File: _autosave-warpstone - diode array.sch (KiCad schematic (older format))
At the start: 89 parts, among them SW1 SW_Push, U1 ProMicro

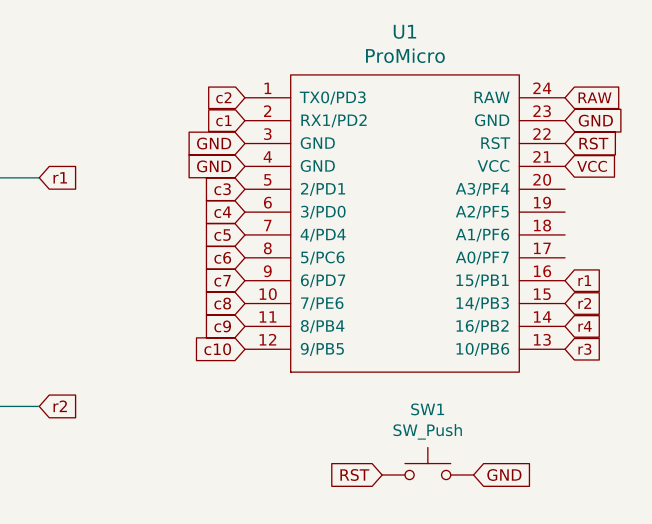
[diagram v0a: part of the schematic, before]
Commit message: overhaul
total overhaul to the design of the board
case design now available
protos en route
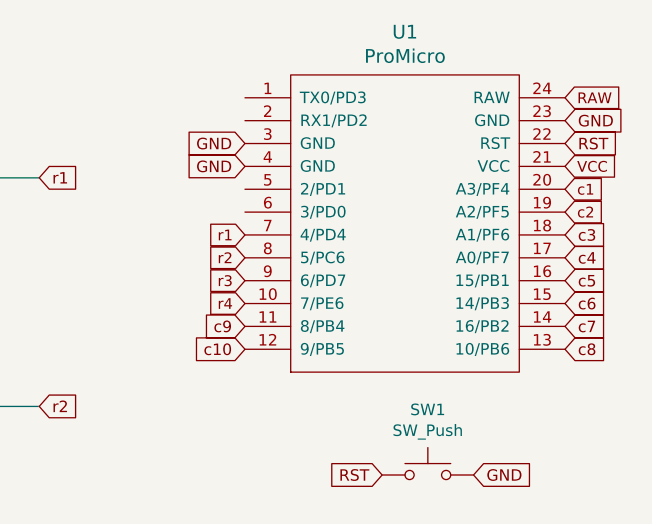
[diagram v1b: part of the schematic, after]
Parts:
- D1, D10, D11, D12, D13, D14, D15, D16, D17, D18, D19, D2, D20, D21, D22, D23, D24, D25, D26, D27, D28, D29, D3, D30, D31, D32, D33, D34, D35, D36, D37, D38, D4, D5, D6, D7, D8, D9: footprint Keebio-Parts:Diode-Hybrid-Back -> Keebio-Parts:D_SOD123
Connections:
- net c1: now also U1.20 (A3/PF4); no longer U1.2 (RX1/PD2)
- net c2: now also U1.19 (A2/PF5); no longer U1.1 (TX0/PD3)
- net c3: now also U1.18 (A1/PF6); no longer U1.5 (2/PD1)
- net c4: now also U1.17 (A0/PF7); no longer U1.6 (3/PD0)
- net c5: now also U1.16 (15/PB1); no longer U1.7 (4/PD4)
- net c6: now also U1.15 (14/PB3); no longer U1.8 (5/PC6)
- net c7: now also U1.14 (16/PB2); no longer U1.9 (6/PD7)
- net c8: now also U1.13 (10/PB6); no longer U1.10 (7/PE6)
- net r1: now also U1.7 (4/PD4); no longer U1.16 (15/PB1)
- net r2: now also U1.8 (5/PC6); no longer U1.15 (14/PB3)
- net r3: now also U1.9 (6/PD7); no longer U1.13 (10/PB6)
- net r4: now also U1.10 (7/PE6); no longer U1.14 (16/PB2)
